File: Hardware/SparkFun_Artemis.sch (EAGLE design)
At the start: 74 parts, among them J1 PAD.4X.6, J10 PAD.4X.6, J11 PAD.4X.6, J12 PAD.4X.6, J13 PAD.4X.6, J14 PAD.4X.6, J15 PAD.4X.6, J16 PAD.4X.6, J17 PAD.4X.6, J18 PAD.4X.6, J19 PAD.4X.6, J2 PAD.4X.6, J20 PAD.4X.6, J21 PAD.4X.6, J22 PAD.4X.6, J23 PAD.4X.6, J24 PAD.4X.6, J25 PAD.4X.6, J26 PAD.4X.6, J27 PAD.4X.6, J28 PAD.4X.6, J29 PAD.4X.6, J3 PAD.4X.6, J30 PAD.4X.6, J31 PAD.4X.6, J32 PAD.4X.6, J34 PAD.4X.6, J35 PAD.4X.6, J36 PAD.4X.6, J37 PAD.4X.6, J38 PAD.4X.6, J39 PAD.4X.6, J4 PAD.4X.6, J40 PAD.4X.6, J41 PAD.4X.6, J42 PAD.4X.6, J43 PAD.4X.6, J44 PAD.4X.6, J45 PAD.4X.6, J46 PAD.35X.35, J47 PAD.4X.6, J48 PAD.4X.6, J49 PAD.4X.6, J5 PAD.4X.6, J6 PAD.4X.6, J7 PAD.4X.6, J8 PAD.4X.6, J9 PAD.4X.6, U1 AMBIQ-APOLLO3KBR, Y1 32MHz

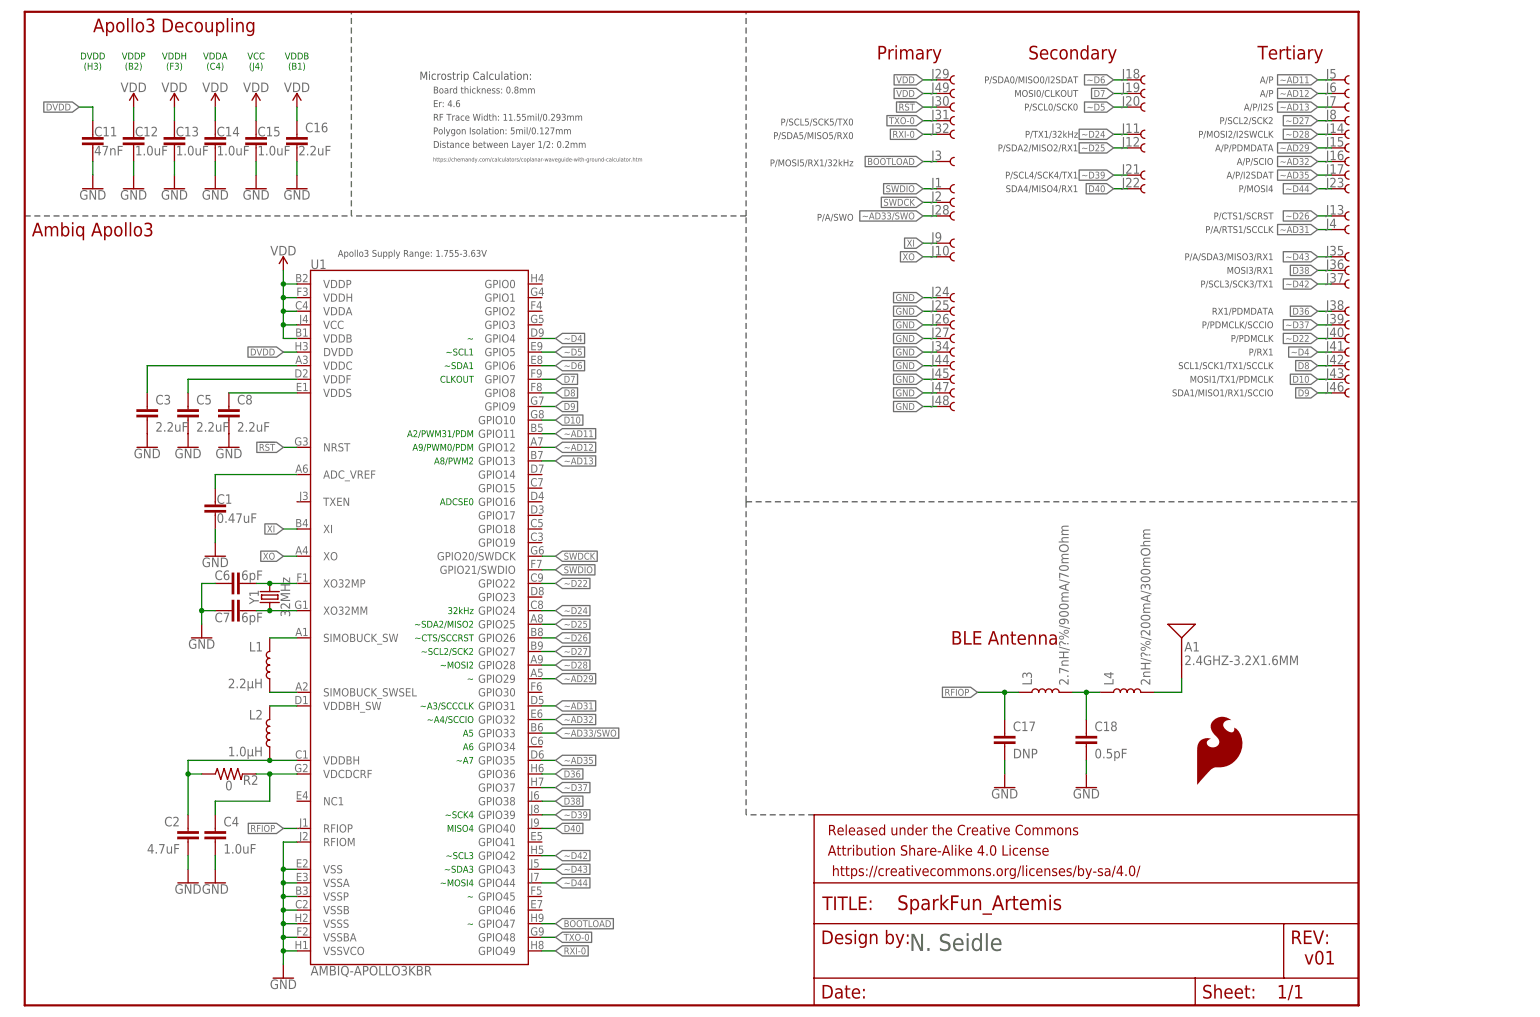
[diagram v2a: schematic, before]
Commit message: Going to buried vias
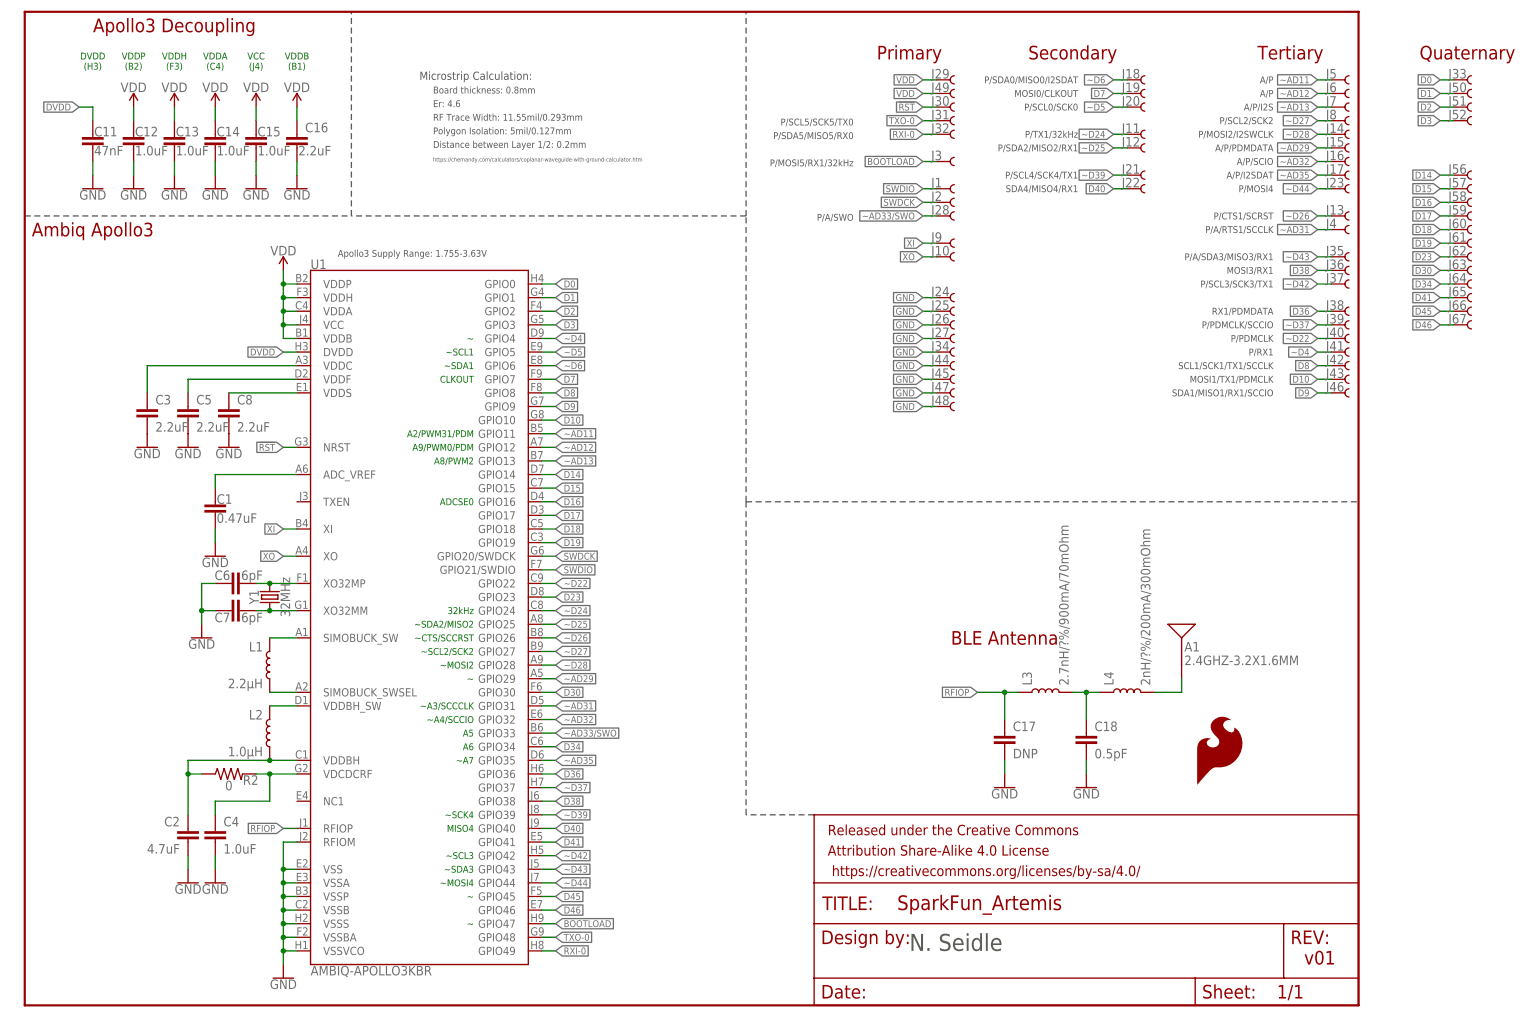
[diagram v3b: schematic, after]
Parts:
- added J33, J50, J51, J52, J56, J57, J58, J59, J60, J61, J62, J63, J64, J65, J66, J67: PAD.4X.6, Module-Pads:PAD.4X.6
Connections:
- new net D0: J33.1, U1.GPIO0
- new net D1: J50.1, U1.GPIO1
- new net D14: J56.1, U1.GPIO14
- new net D15: J57.1, U1.GPIO15
- new net D16: J58.1, U1.GPIO16
- new net D17: J59.1, U1.GPIO17
- new net D18: J60.1, U1.GPIO18
- new net D19: J61.1, U1.GPIO19
- new net D2: J51.1, U1.GPIO2
- new net D23: J62.1, U1.GPIO23
- new net D3: J52.1, U1.GPIO3
- new net D30: J63.1, U1.GPIO30
- new net D34: J64.1, U1.GPIO34
- new net D41: J65.1, U1.GPIO41
- new net D45: J66.1, U1.GPIO45
- new net D46: J67.1, U1.GPIO46
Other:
- note added: "Quaternary"

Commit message: Buried via approach. Moar GPIOs!
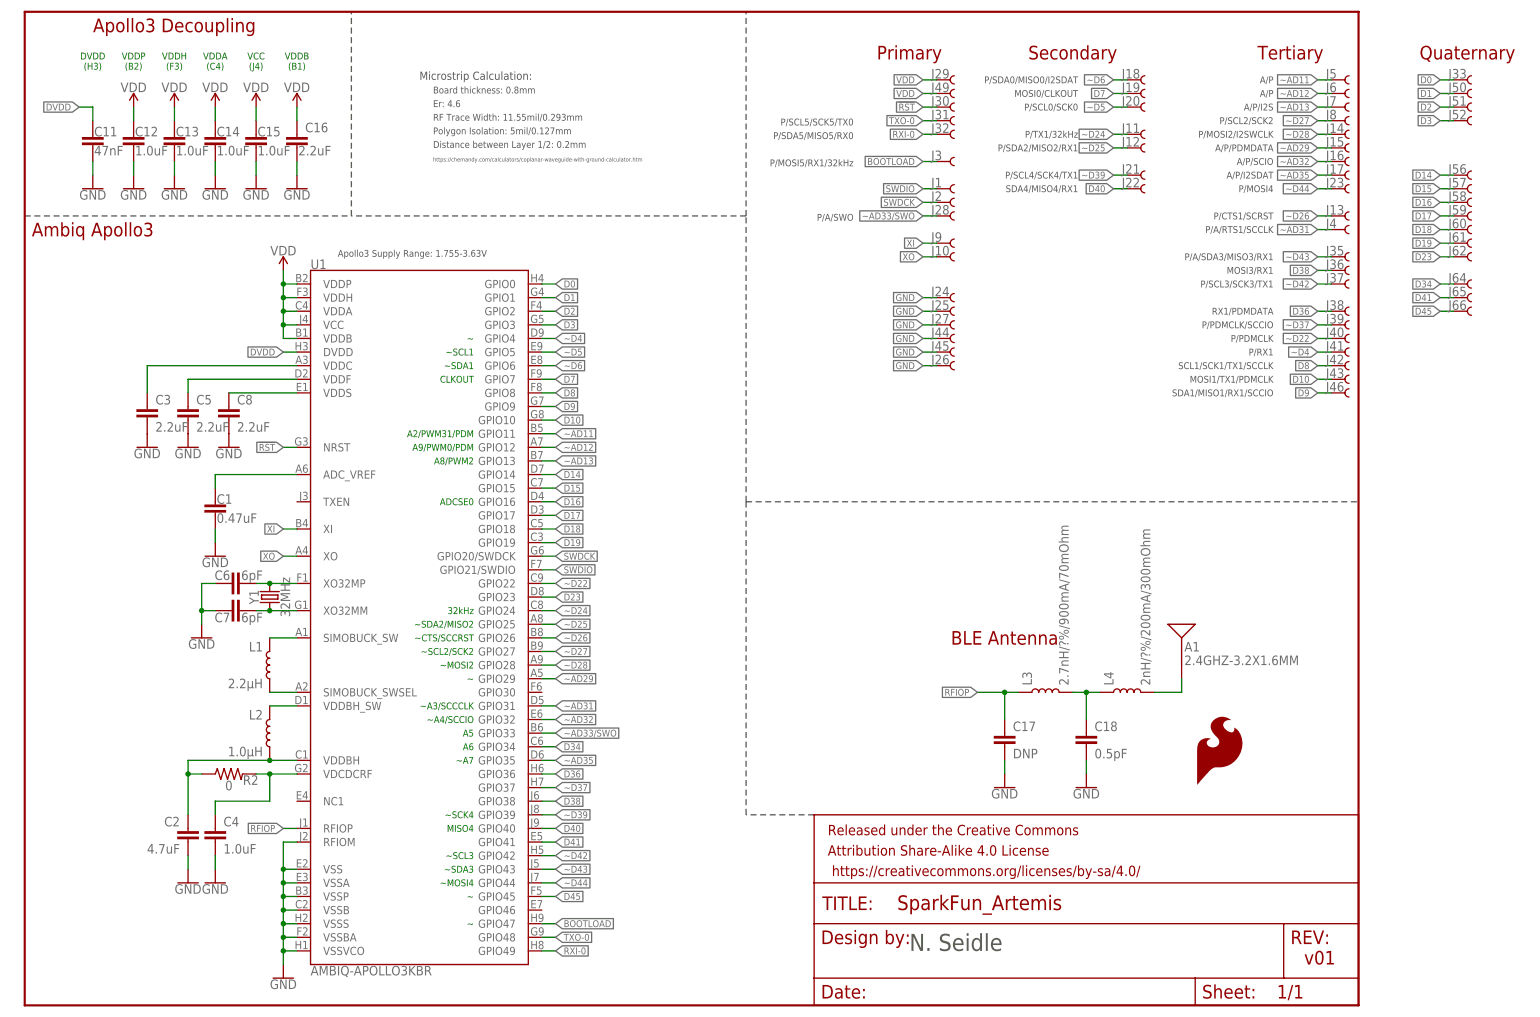
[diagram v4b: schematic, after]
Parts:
- removed J34, J47, J48, J63, J67: PAD.4X.6, Module-Pads:PAD.4X.6
- J27, J44: value PAD.4X.6 -> PAD.35X.35; device Module-Pads:PAD.4X.6 -> Module-Pads:PAD.35X.35
- J46: value PAD.35X.35 -> PAD.4X.6; device Module-Pads:PAD.35X.35 -> Module-Pads:PAD.4X.6
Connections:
- removed net D30: J63.1, U1.GPIO30
- removed net D46: J67.1, U1.GPIO46
- net GND: no longer J34.1, J47.1, J48.1
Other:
- moved on the sheet: J26, J27, J44, J45

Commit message: Commit for Quote
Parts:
- removed J60, J61, J62, J64, J65, J66: PAD.4X.6, Module-Pads:PAD.4X.6
- added J34, J47, J48, J53, J54, J55: PAD.4X.6, Module-Pads:PAD.4X.6
- J22, J38: value PAD.4X.6 -> PAD.35X.35; device Module-Pads:PAD.4X.6 -> Module-Pads:PAD.35X.35
- J27, J44: value PAD.35X.35 -> PAD.4X.6; device Module-Pads:PAD.35X.35 -> Module-Pads:PAD.4X.6
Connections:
- net !RST: now also J50.1; no longer J30.1
- net BOOTLOAD: now also J7.1; no longer J3.1
- net D0: now also J51.1; no longer J33.1
- net D1: now also J49.1; no longer J50.1
- net D10: now also J8.1; no longer J43.1
- net D14: now also J20.1; no longer J56.1
- net D15: now also J29.1; no longer J57.1
- net D16: now also J42.1; no longer J58.1
- net D17: now also J43.1; no longer J59.1
- net D18: now also J41.1; no longer J60.1
- net D19: now also J40.1; no longer J61.1
- net D2: now also J48.1; no longer J51.1
- net D23: now also J18.1; no longer J62.1
- net D3: now also J54.1; no longer J52.1
- net D34: now also J31.1; no longer J64.1
- net D36: now also J55.1; no longer J38.1
- net D38: now also J56.1; no longer J36.1
- net D40: now also J5.1; no longer J22.1
- net D41: now also J45.1; no longer J65.1
- net D45: now also J46.1; no longer J66.1
- net D7: now also J13.1; no longer J19.1
- net D8: now also J11.1; no longer J42.1
- net D9: now also J6.1; no longer J46.1
- net GND: now also J1.1, J22.1, J38.1, J39.1, J47.1, J59.1; no longer J24.1, J25.1, J26.1, J27.1, J44.1, J45.1
- net RXI-0: now also J3.1; no longer J32.1
- net SWDIO: now also J10.1; no longer J1.1
- net TXO-0: now also J9.1; no longer J31.1
- net VDD: now also J36.1, J37.1; no longer J29.1, J49.1
- net XI: now also J35.1; no longer J9.1
- net XO: now also J34.1; no longer J10.1
- net ~AD11: now also J32.1; no longer J5.1
- net ~AD12: now also J26.1; no longer J6.1
- net ~AD13: now also J28.1; no longer J7.1
- net ~AD29: now also J33.1; no longer J15.1
- net ~AD31: now also J44.1; no longer J4.1
- net ~AD32: now also J24.1; no longer J16.1
- net ~AD33/SWO: now also J30.1; no longer J28.1
- net ~AD35: now also J14.1; no longer J17.1
- net ~D22: now also J17.1; no longer J40.1
- net ~D24: now also J16.1; no longer J11.1
- net ~D25: now also J25.1; no longer J12.1
- net ~D26: now also J27.1; no longer J13.1
- net ~D27: now also J19.1; no longer J8.1
- net ~D28: now also J21.1; no longer J14.1
- net ~D37: now also J57.1; no longer J39.1
- net ~D39: now also J4.1; no longer J21.1
- net ~D4: now also J15.1; no longer J41.1
- net ~D42: now also J53.1; no longer J37.1
- net ~D43: now also J52.1; no longer J35.1
- net ~D44: now also J58.1; no longer J23.1
- net ~D5: now also J12.1; no longer J20.1
- net ~D6: now also J23.1; no longer J18.1
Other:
- moved on the sheet: J1, J10, J11, J12, J13, J14, J15, J16, J17, J18, J19, J20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

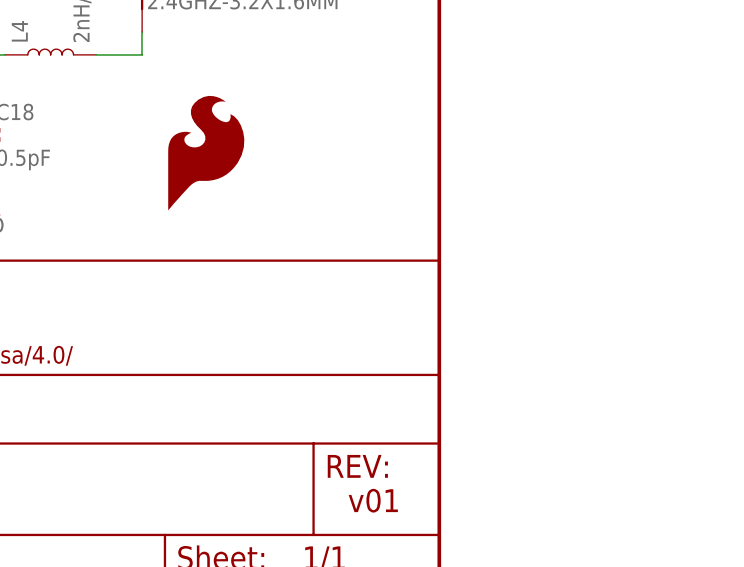
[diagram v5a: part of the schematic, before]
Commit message: Add fiducials. Add auto-bootload timing diagram.
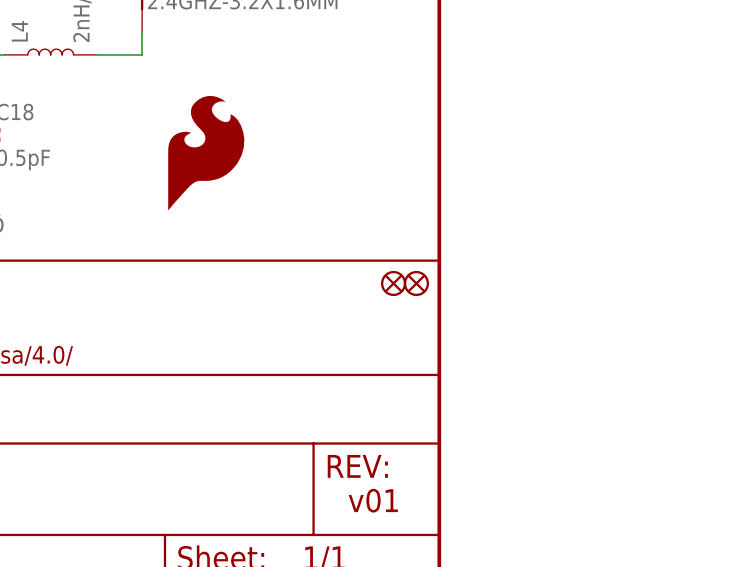
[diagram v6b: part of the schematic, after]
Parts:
- added FD3, FD4: FIDUCIAL0.2MM, SparkFun-Aesthetics:FIDUCIAL0.2MM
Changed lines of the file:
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@@
 <part name="J46" library="Module-Pads" deviceset="PAD" device=".4X.6" value="PAD.4X.6"/>
 <part name="J47" library="Module-Pads" deviceset="PAD" device=".4X.6"/>
+<part name="FD3" library="SparkFun-Aesthetics" deviceset="FIDUCIAL" device="0.2MM"/>
+<part name="FD4" library="SparkFun-Aesthetics" deviceset="FIDUCIAL" device="0.2MM"/>
 </parts>
 <sheets>
@@
 <attribute name="NAME" x="169.164" y="119.634" size="1.778" layer="95" font="vector"/>
 </instance>
+<instance part="FD3" gate="G$1" x="246.38" y="33.02" smashed="yes"/>
+<instance part="FD4" gate="G$1" x="243.84" y="33.02" smashed="yes"/>
 </instances>
 <busses>
